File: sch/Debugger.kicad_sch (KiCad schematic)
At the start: 20 parts, among them J3 USB_C_Receptacle_USB2.0_16P, J8 Conn_ARM_SWD_TagConnect_TC203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, U3 TPD3E001DRLR, U5 nRF52833-QDXX, U6 TXB0106RGY, Y2 32MHz

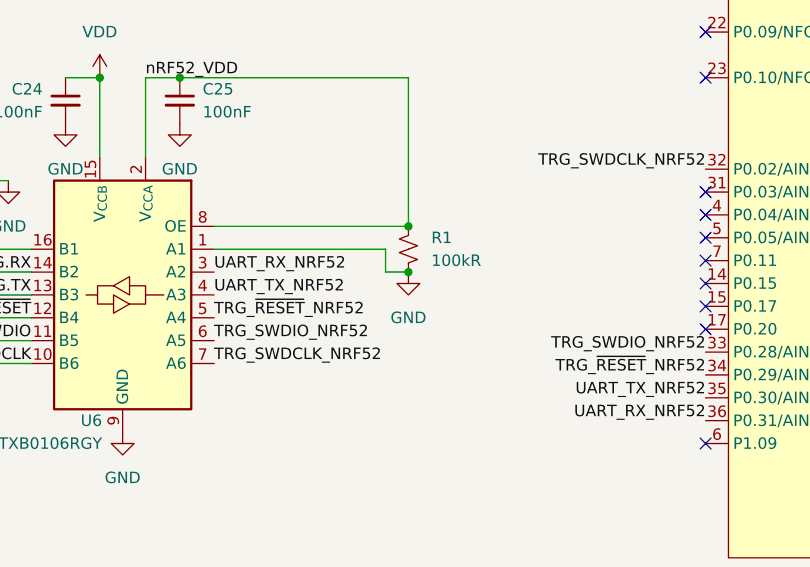
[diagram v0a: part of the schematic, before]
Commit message: Renamed to RoyalBlue54L-Feather
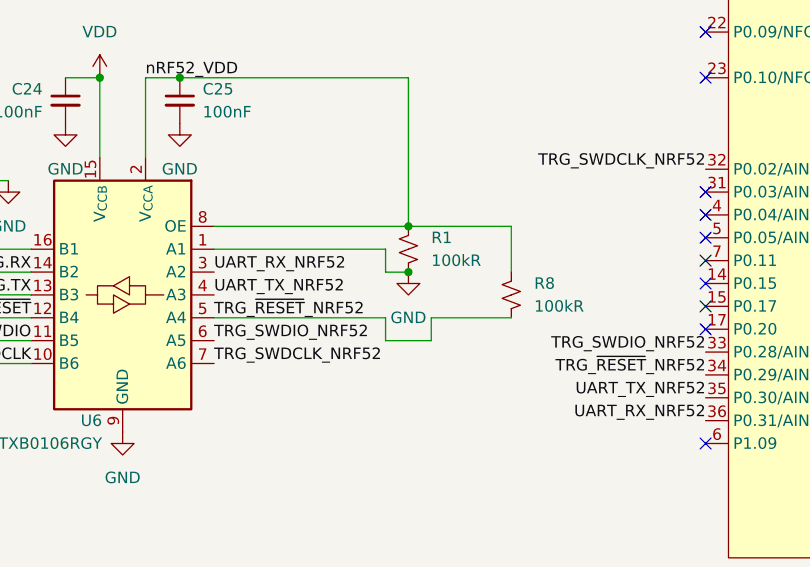
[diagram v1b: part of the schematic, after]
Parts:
- added R8: 100kR, Resistor_SMD:R_0402_1005Metric, symbol Device:R_Small_US
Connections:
- net TRG_~{RESET}_NRF52: now also R8.2
- net nRF52_VDD: now also R8.1

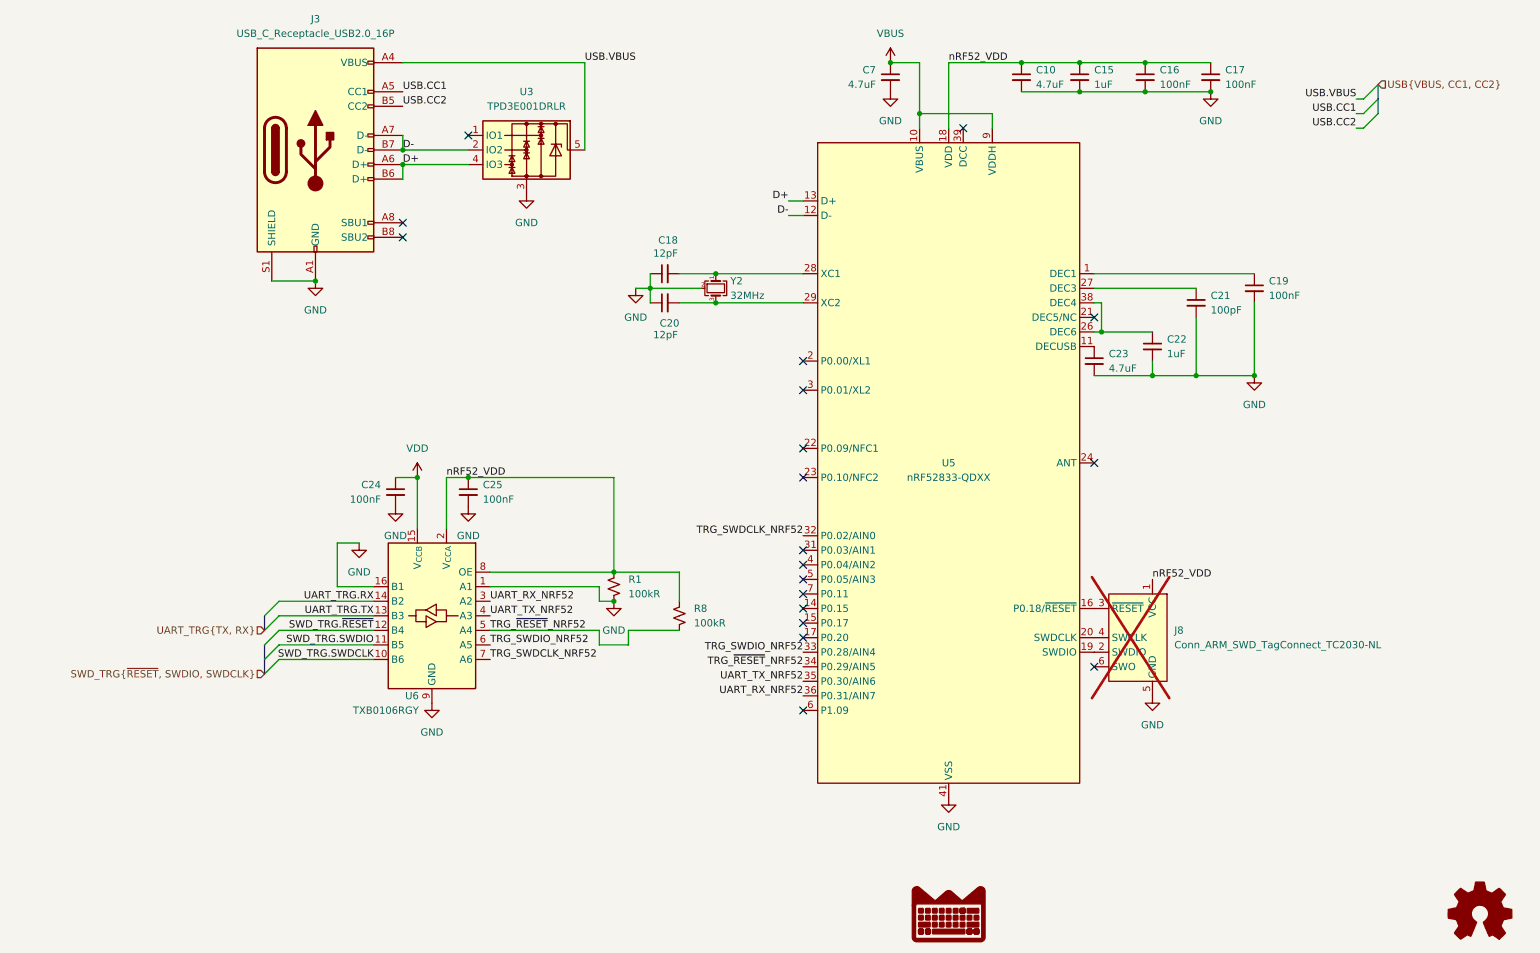
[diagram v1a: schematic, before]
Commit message: Added testpoints, moved USB connection to VSYS.
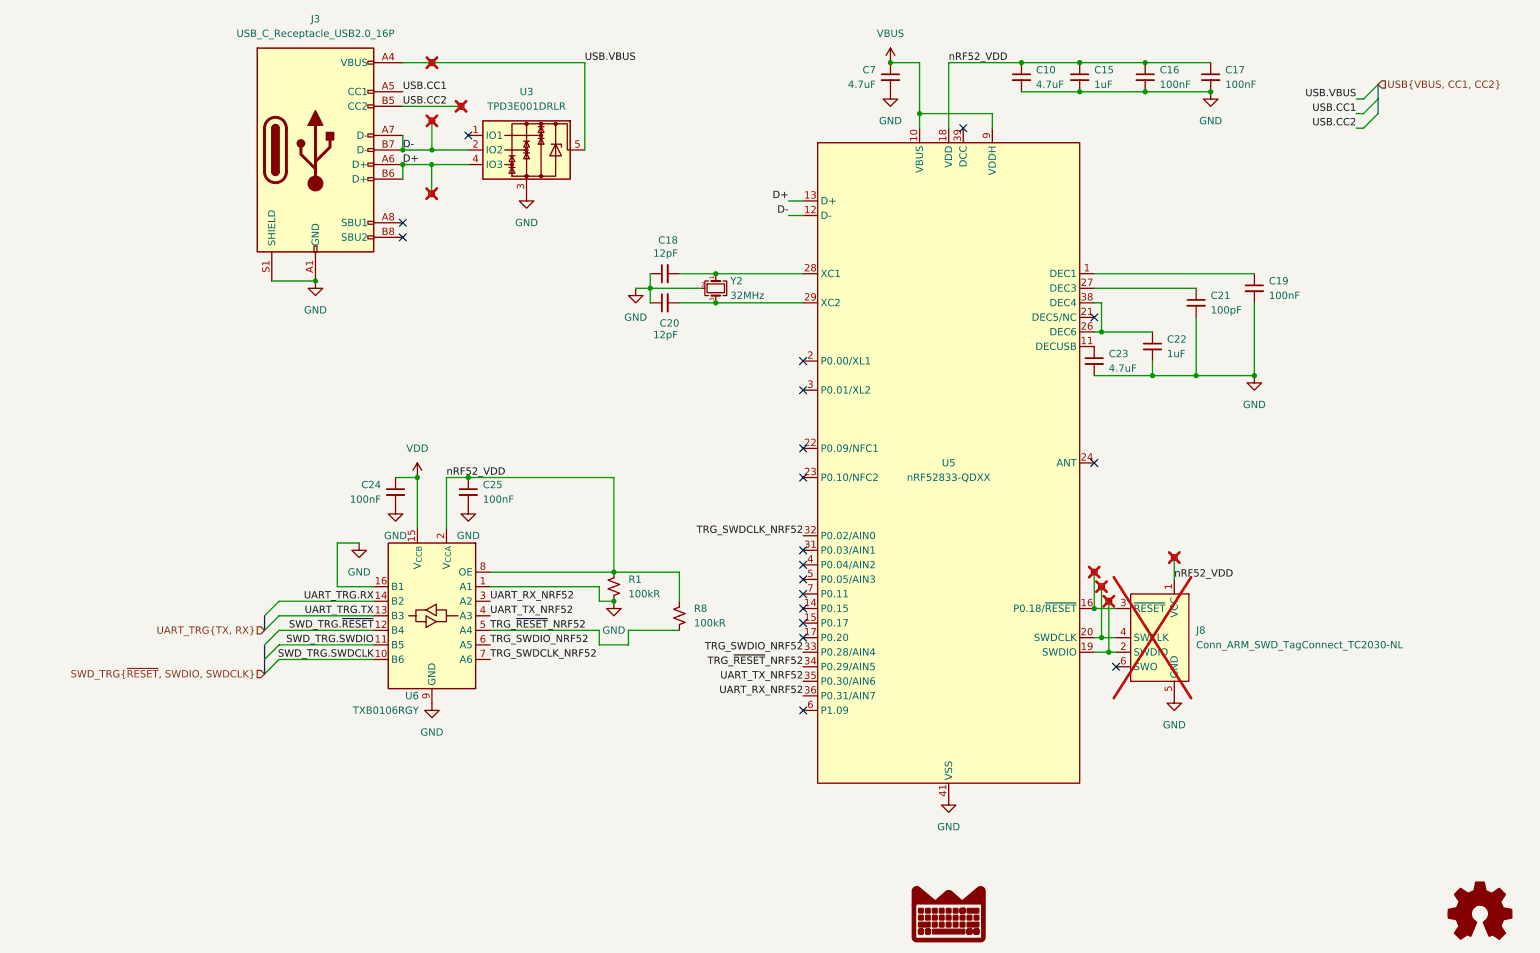
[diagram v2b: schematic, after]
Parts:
- added TP10, TP11, TP12, TP5, TP6, TP7, TP8, TP9: TestPoint, TestPoint:TestPoint_Pad_D1.5mm, symbol Connector:TestPoint_Small
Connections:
- net D+: now also TP7.1
- net D-: now also TP8.1
- net USB.CC2: now also TP6.1
- net USB.VBUS: now also TP5.1
- net nRF52_VDD: now also TP9.1
- net at J8.3 (~{RESET}), U5.16 (P0.18/~{RESET}): now also TP10.1
- net at J8.2 (SWDIO), U5.19 (SWDIO): now also TP12.1
- net at J8.4 (SWCLK), U5.20 (SWDCLK): now also TP11.1
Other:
- moved on the sheet: J8
